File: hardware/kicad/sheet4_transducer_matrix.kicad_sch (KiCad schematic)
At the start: 0 parts

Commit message: feat: populate all 4 KiCad schematic sheets with embedded symbols and wiring
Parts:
- added TX1, TX10, TX11, TX12, TX13, TX14, TX15, TX16, TX17, TX18, TX19, TX2, TX20, TX21, TX22, TX23, TX24, TX25, TX26, TX27, TX28, TX29, TX3, TX30, TX31, TX32, TX33, TX34, TX35, TX36, TX37, TX38, TX39, TX4, TX40, TX41, TX42, TX43, TX44, TX45, TX46, TX47, TX48, TX49, TX5, TX50, TX51, TX52, TX53, TX54, TX55, TX56, TX57, TX58, TX59, TX6, TX60, TX61, TX62, TX63, TX64, TX7, TX8, TX9: 400ST160, symbol HPVE:Transducer_400ST
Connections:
- new net DRV_1: TX1.1 (+)
- new net DRV_10: TX10.1 (+)
- new net DRV_11: TX11.1 (+)
- new net DRV_12: TX12.1 (+)
- new net DRV_13: TX13.1 (+)
- new net DRV_14: TX14.1 (+)
- new net DRV_15: TX15.1 (+)
- new net DRV_16: TX16.1 (+)
- new net DRV_17: TX17.1 (+)
- new net DRV_18: TX18.1 (+)
- new net DRV_19: TX19.1 (+)
- new net DRV_2: TX2.1 (+)
- new net DRV_20: TX20.1 (+)
- new net DRV_21: TX21.1 (+)
- new net DRV_22: TX22.1 (+)
- new net DRV_23: TX23.1 (+)
- new net DRV_24: TX24.1 (+)
- new net DRV_25: TX25.1 (+)
- new net DRV_26: TX26.1 (+)
- new net DRV_27: TX27.1 (+)
- new net DRV_28: TX28.1 (+)
- new net DRV_29: TX29.1 (+)
- new net DRV_3: TX3.1 (+)
- new net DRV_30: TX30.1 (+)
- new net DRV_31: TX31.1 (+)
- new net DRV_32: TX32.1 (+)
- new net DRV_33: TX33.1 (+)
- new net DRV_34: TX34.1 (+)
- new net DRV_35: TX35.1 (+)
- new net DRV_36: TX36.1 (+)
- new net DRV_37: TX37.1 (+)
- new net DRV_38: TX38.1 (+)
- new net DRV_39: TX39.1 (+)
- new net DRV_4: TX4.1 (+)
- new net DRV_40: TX40.1 (+)
- new net DRV_41: TX41.1 (+)
- new net DRV_42: TX42.1 (+)
- new net DRV_43: TX43.1 (+)
- new net DRV_44: TX44.1 (+)
- new net DRV_45: TX45.1 (+)
- new net DRV_46: TX46.1 (+)
- new net DRV_47: TX47.1 (+)
- new net DRV_48: TX48.1 (+)
- new net DRV_49: TX49.1 (+)
- new net DRV_5: TX5.1 (+)
- new net DRV_50: TX50.1 (+)
- new net DRV_51: TX51.1 (+)
- new net DRV_52: TX52.1 (+)
- new net DRV_53: TX53.1 (+)
- new net DRV_54: TX54.1 (+)
- new net DRV_55: TX55.1 (+)
- new net DRV_56: TX56.1 (+)
- new net DRV_57: TX57.1 (+)
- new net DRV_58: TX58.1 (+)
- new net DRV_59: TX59.1 (+)
- new net DRV_6: TX6.1 (+)
- new net DRV_60: TX60.1 (+)
- new net DRV_61: TX61.1 (+)
- new net DRV_62: TX62.1 (+)
- new net DRV_63: TX63.1 (+)
- new net DRV_64: TX64.1 (+)
- new net DRV_7: TX7.1 (+)
- new net DRV_8: TX8.1 (+)
- new net DRV_9: TX9.1 (+)
- new net GND: TX1.2 (-), TX10.2 (-), TX11.2 (-), TX12.2 (-), TX13.2 (-), TX14.2 (-), TX15.2 (-), TX16.2 (-), TX17.2 (-), TX18.2 (-), TX19.2 (-), TX2.2 (-), TX20.2 (-), TX21.2 (-), TX22.2 (-), TX23.2 (-), TX24.2 (-), TX25.2 (-), TX26.2 (-), TX27.2 (-), TX28.2 (-), TX29.2 (-), TX3.2 (-), TX30.2 (-), TX31.2 (-), TX32.2 (-), TX33.2 (-), TX34.2 (-), TX35.2 (-), TX36.2 (-), TX37.2 (-), TX38.2 (-), TX39.2 (-), TX4.2 (-), TX40.2 (-), TX41.2 (-), TX42.2 (-), TX43.2 (-), TX44.2 (-), TX45.2 (-), TX46.2 (-), TX47.2 (-), TX48.2 (-), TX49.2 (-), TX5.2 (-), TX50.2 (-), TX51.2 (-), TX52.2 (-), TX53.2 (-), TX54.2 (-), TX55.2 (-), TX56.2 (-), TX57.2 (-), TX58.2 (-), TX59.2 (-), TX6.2 (-), TX60.2 (-), TX61.2 (-), TX62.2 (-), TX63.2 (-), TX64.2 (-), TX7.2 (-), TX8.2 (-), TX9.2 (-)
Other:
- title: Sheet 4: 8x8 Transducer Matrix Grid -> Sheet 4: 8x8 Transducer Matrix Grid (64 Elements)

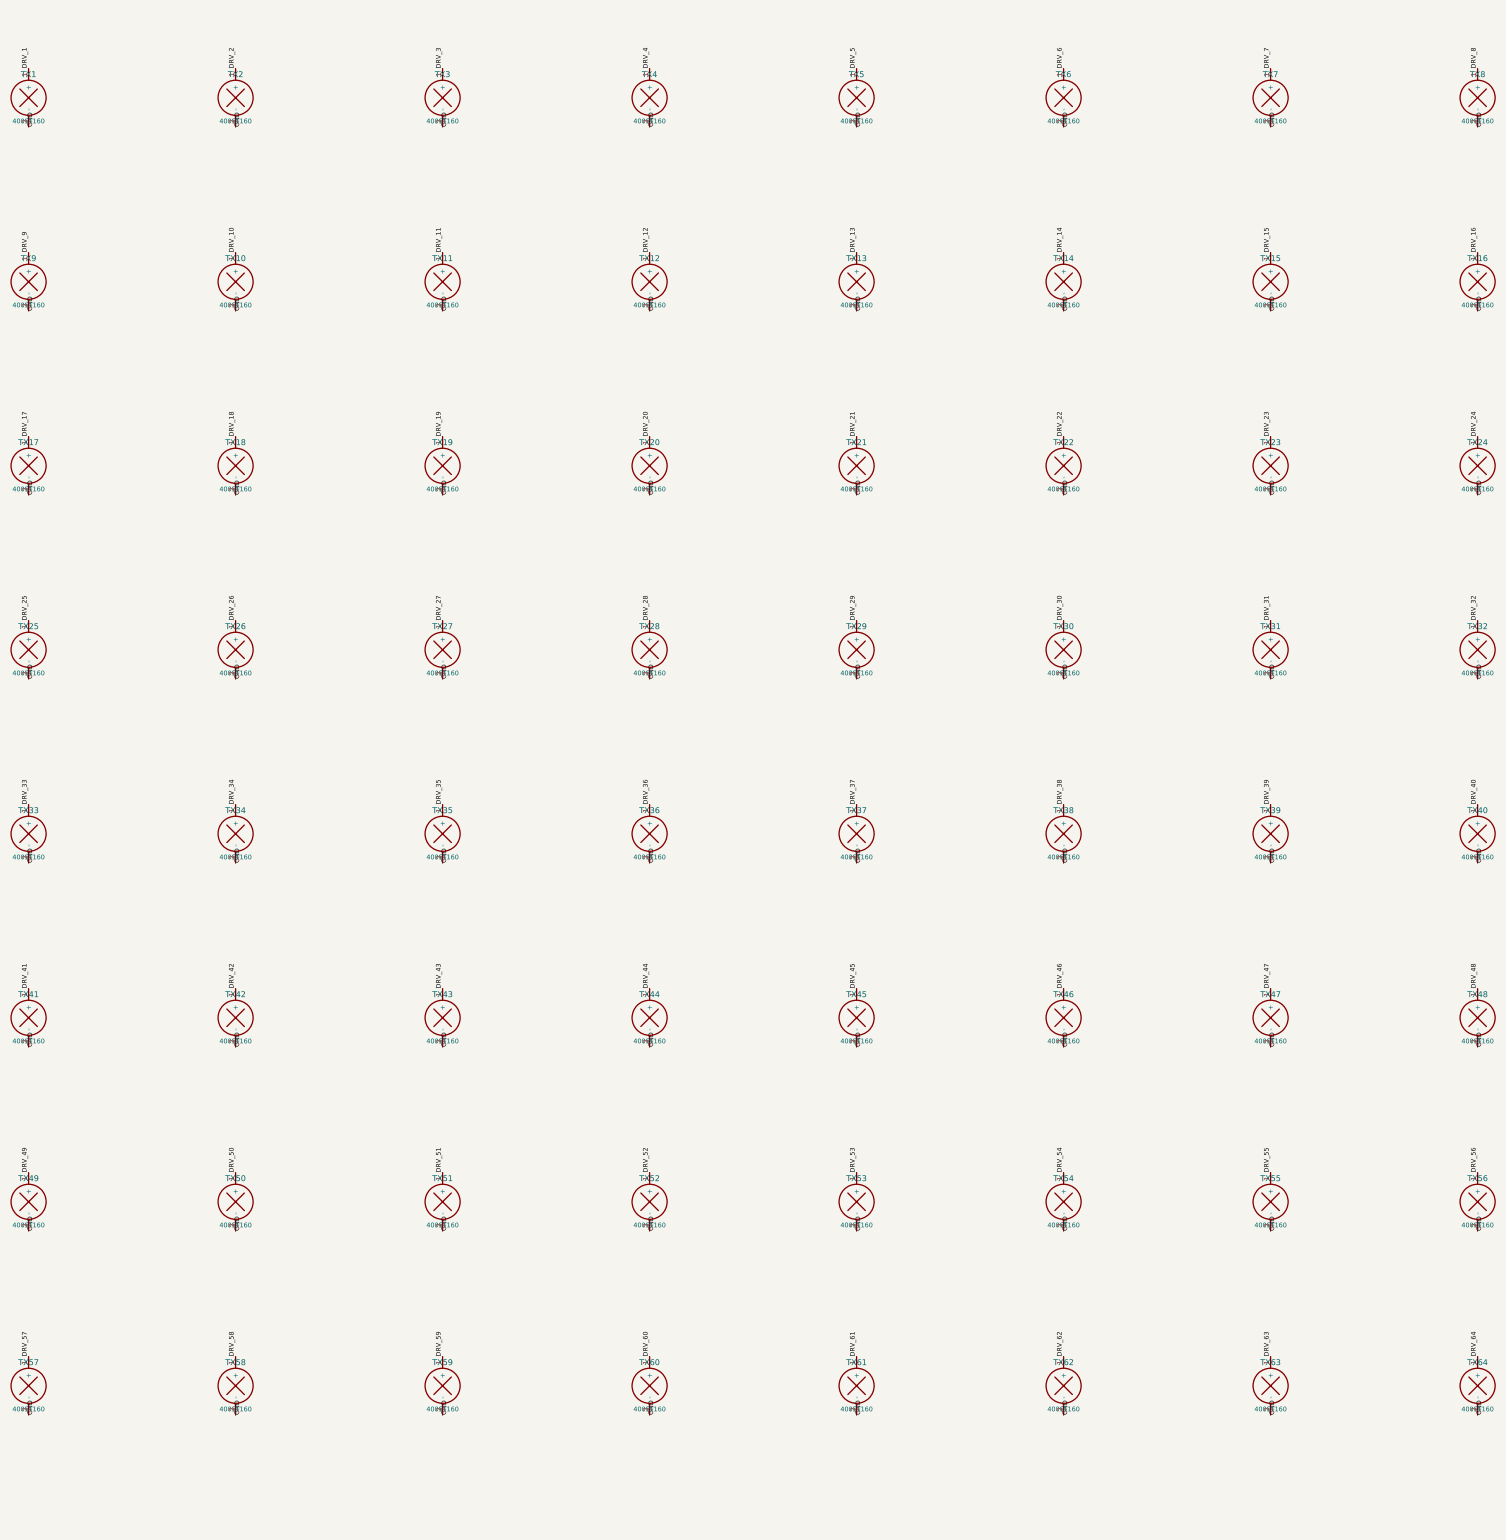
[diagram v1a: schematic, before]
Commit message: fix(kicad): assign valid footprints to all 105 symbols and add visible wiring
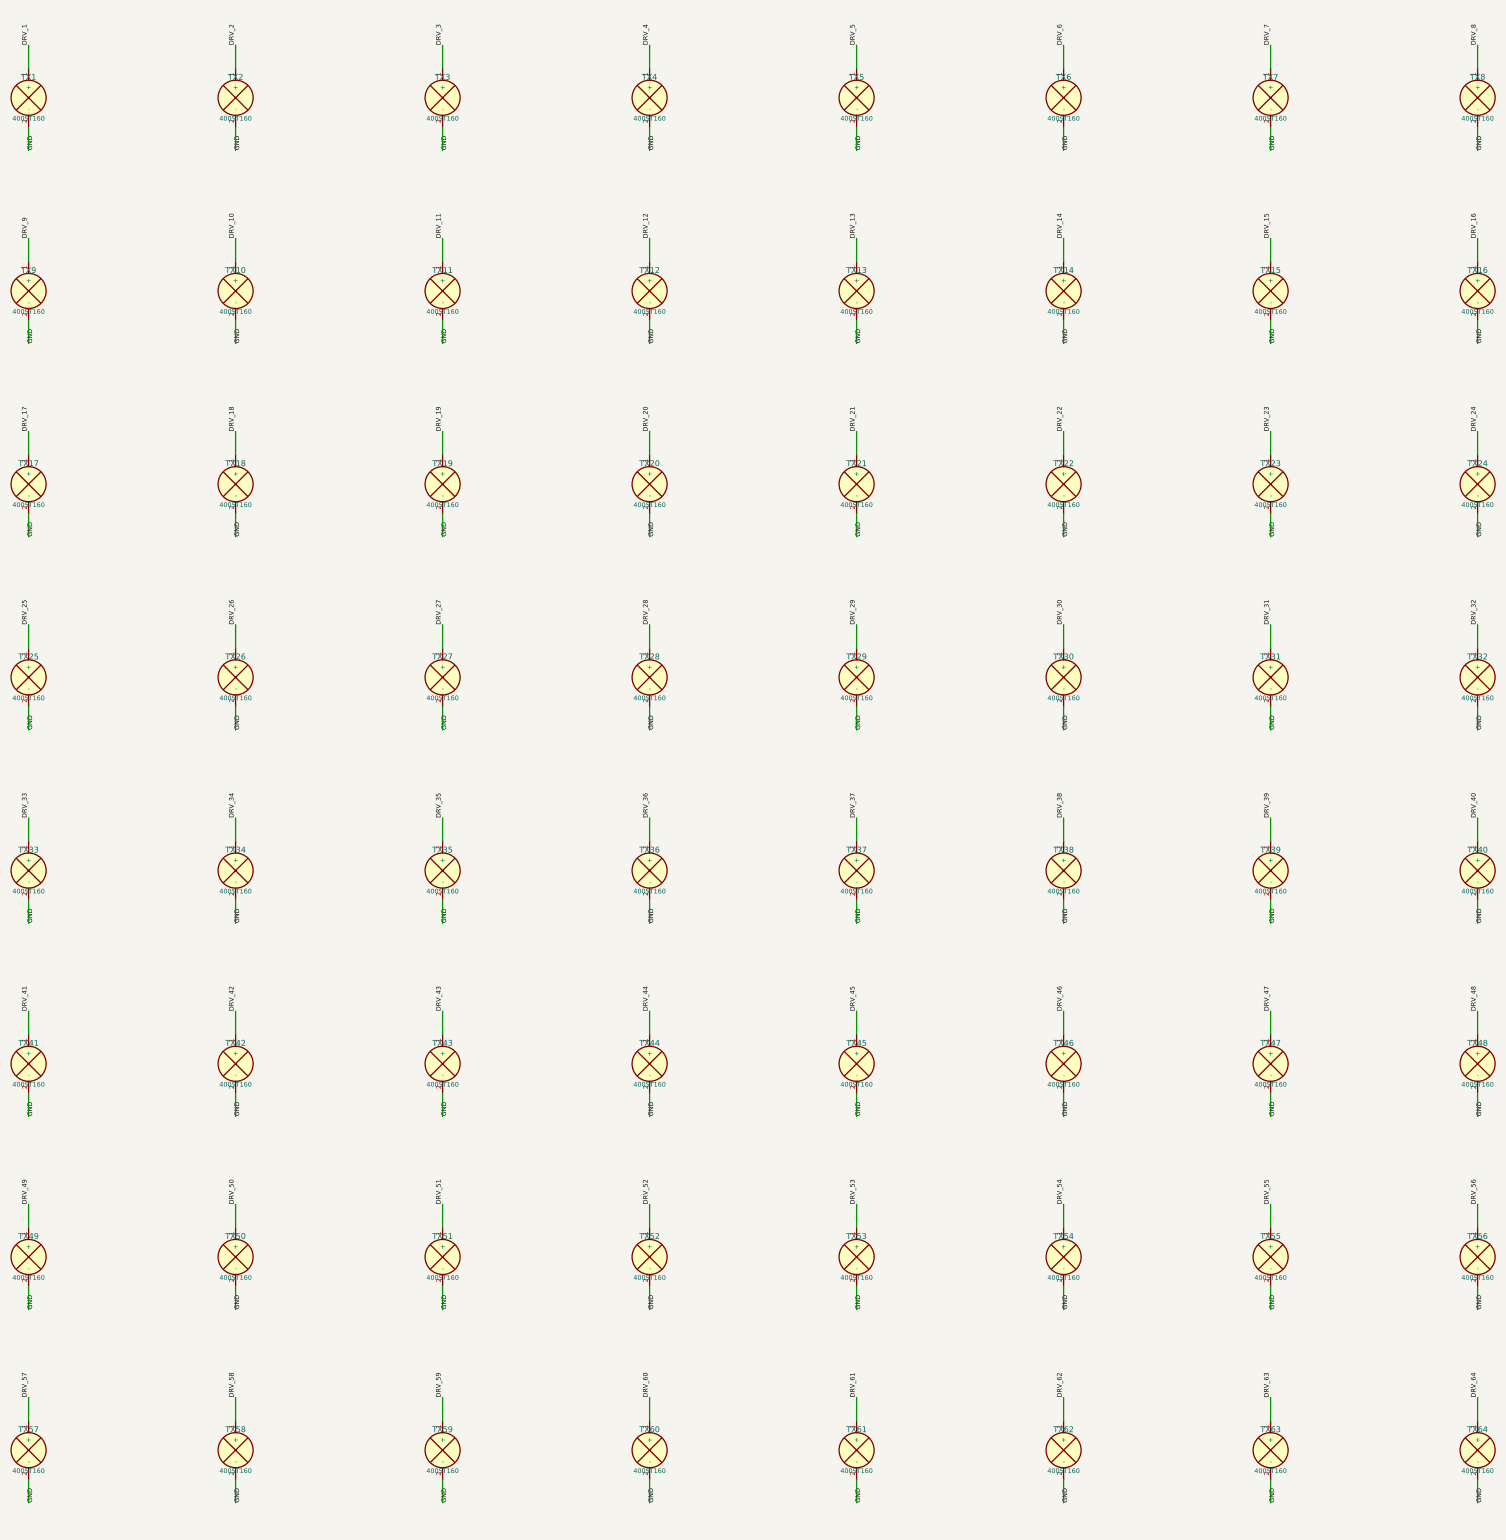
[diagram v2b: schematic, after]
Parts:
- TX1, TX10, TX11, TX12, TX13, TX14, TX15, TX16, TX17, TX18, TX19, TX2, TX20, TX21, TX22, TX23, TX24, TX25, TX26, TX27, TX28, TX29, TX3, TX30, TX31, TX32, TX33, TX34, TX35, TX36, TX37, TX38, TX39, TX4, TX40, TX41, TX42, TX43, TX44, TX45, TX46, TX47, TX48, TX49, TX5, TX50, TX51, TX52, TX53, TX54, TX55, TX56, TX57, TX58, TX59, TX6, TX60, TX61, TX62, TX63, TX64, TX7, TX8, TX9: footprint (none) -> Connector_PinHeader_2.54mm:PinHeader_1x02_P2.54mm_Vertical

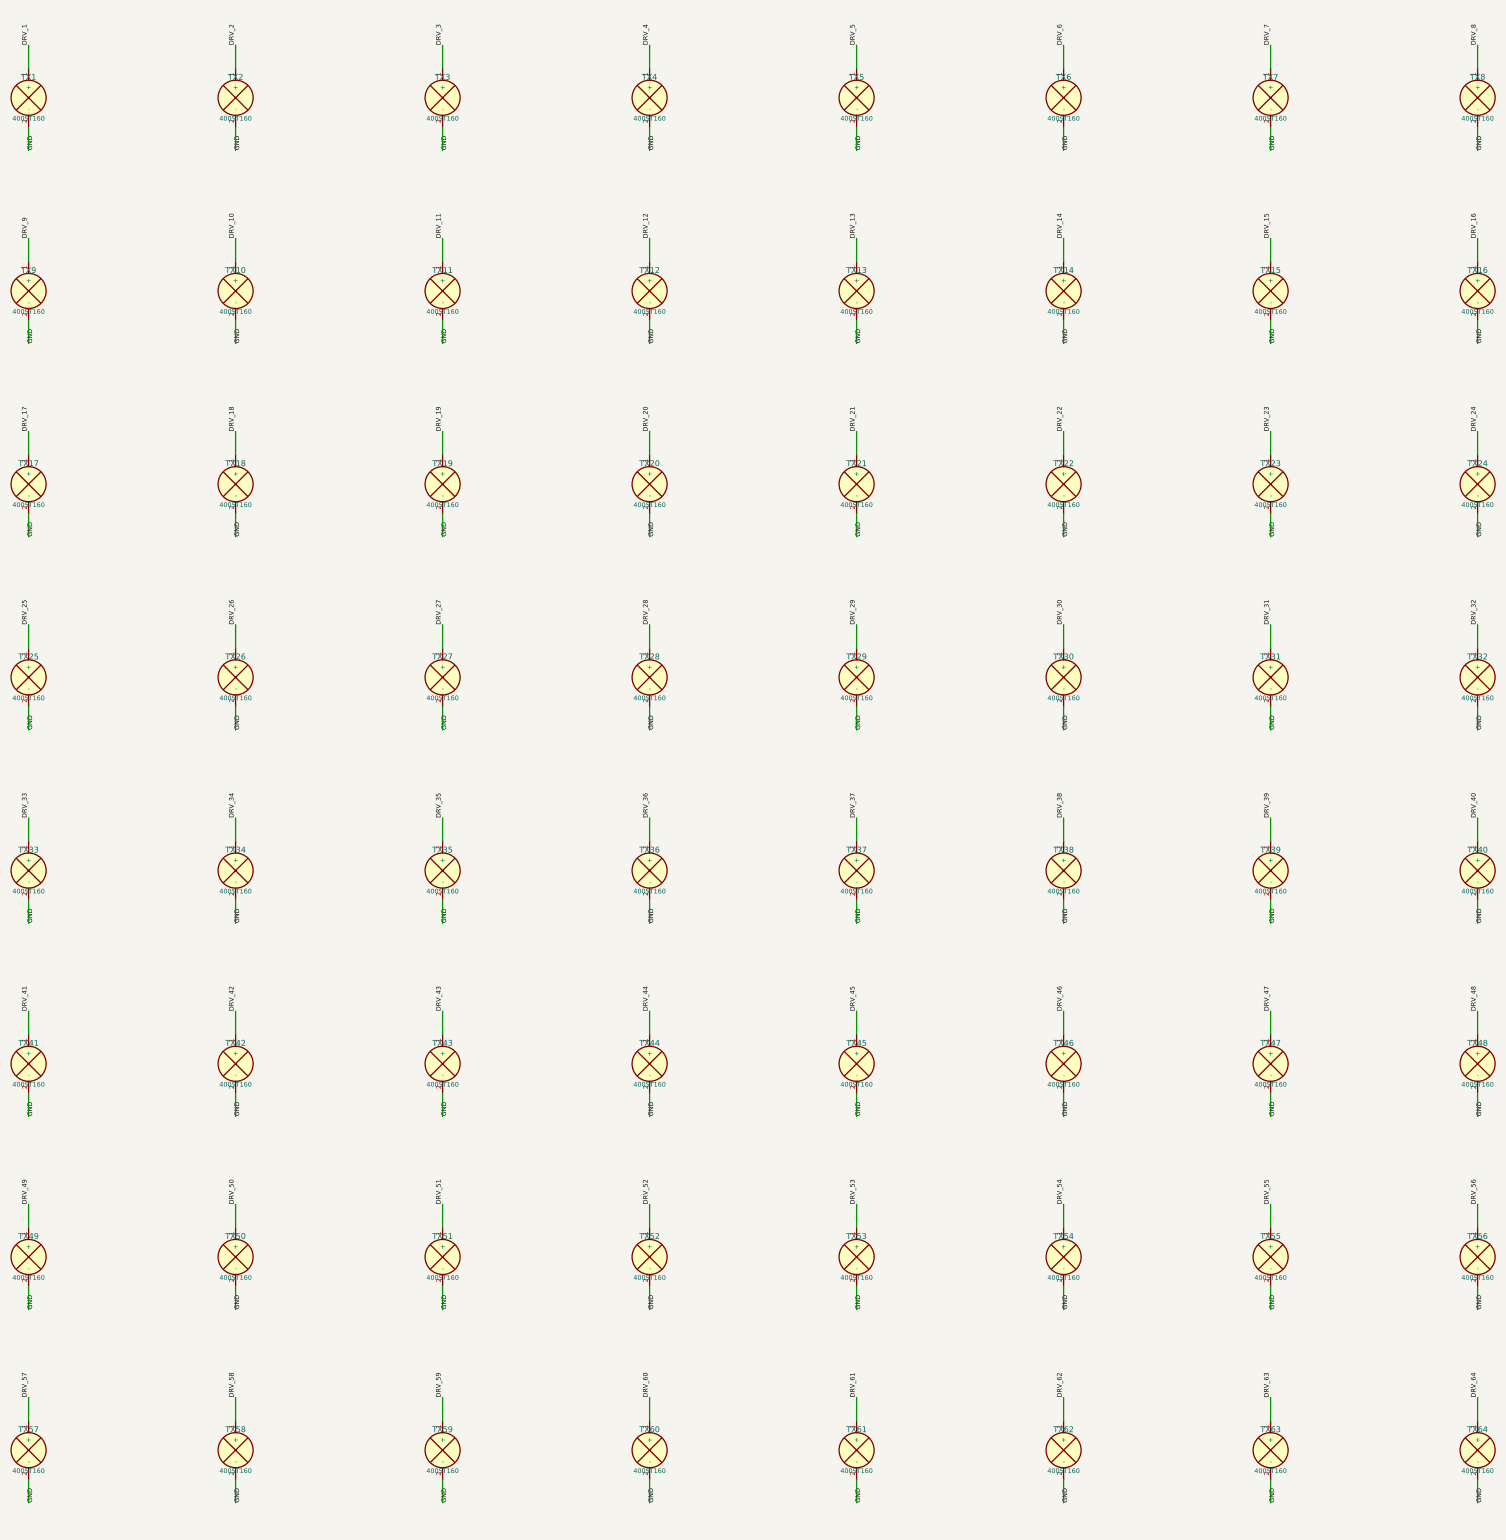
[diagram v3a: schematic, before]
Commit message: Auto-route 392 copper tracks for 64-channel HPVE phased array PCB
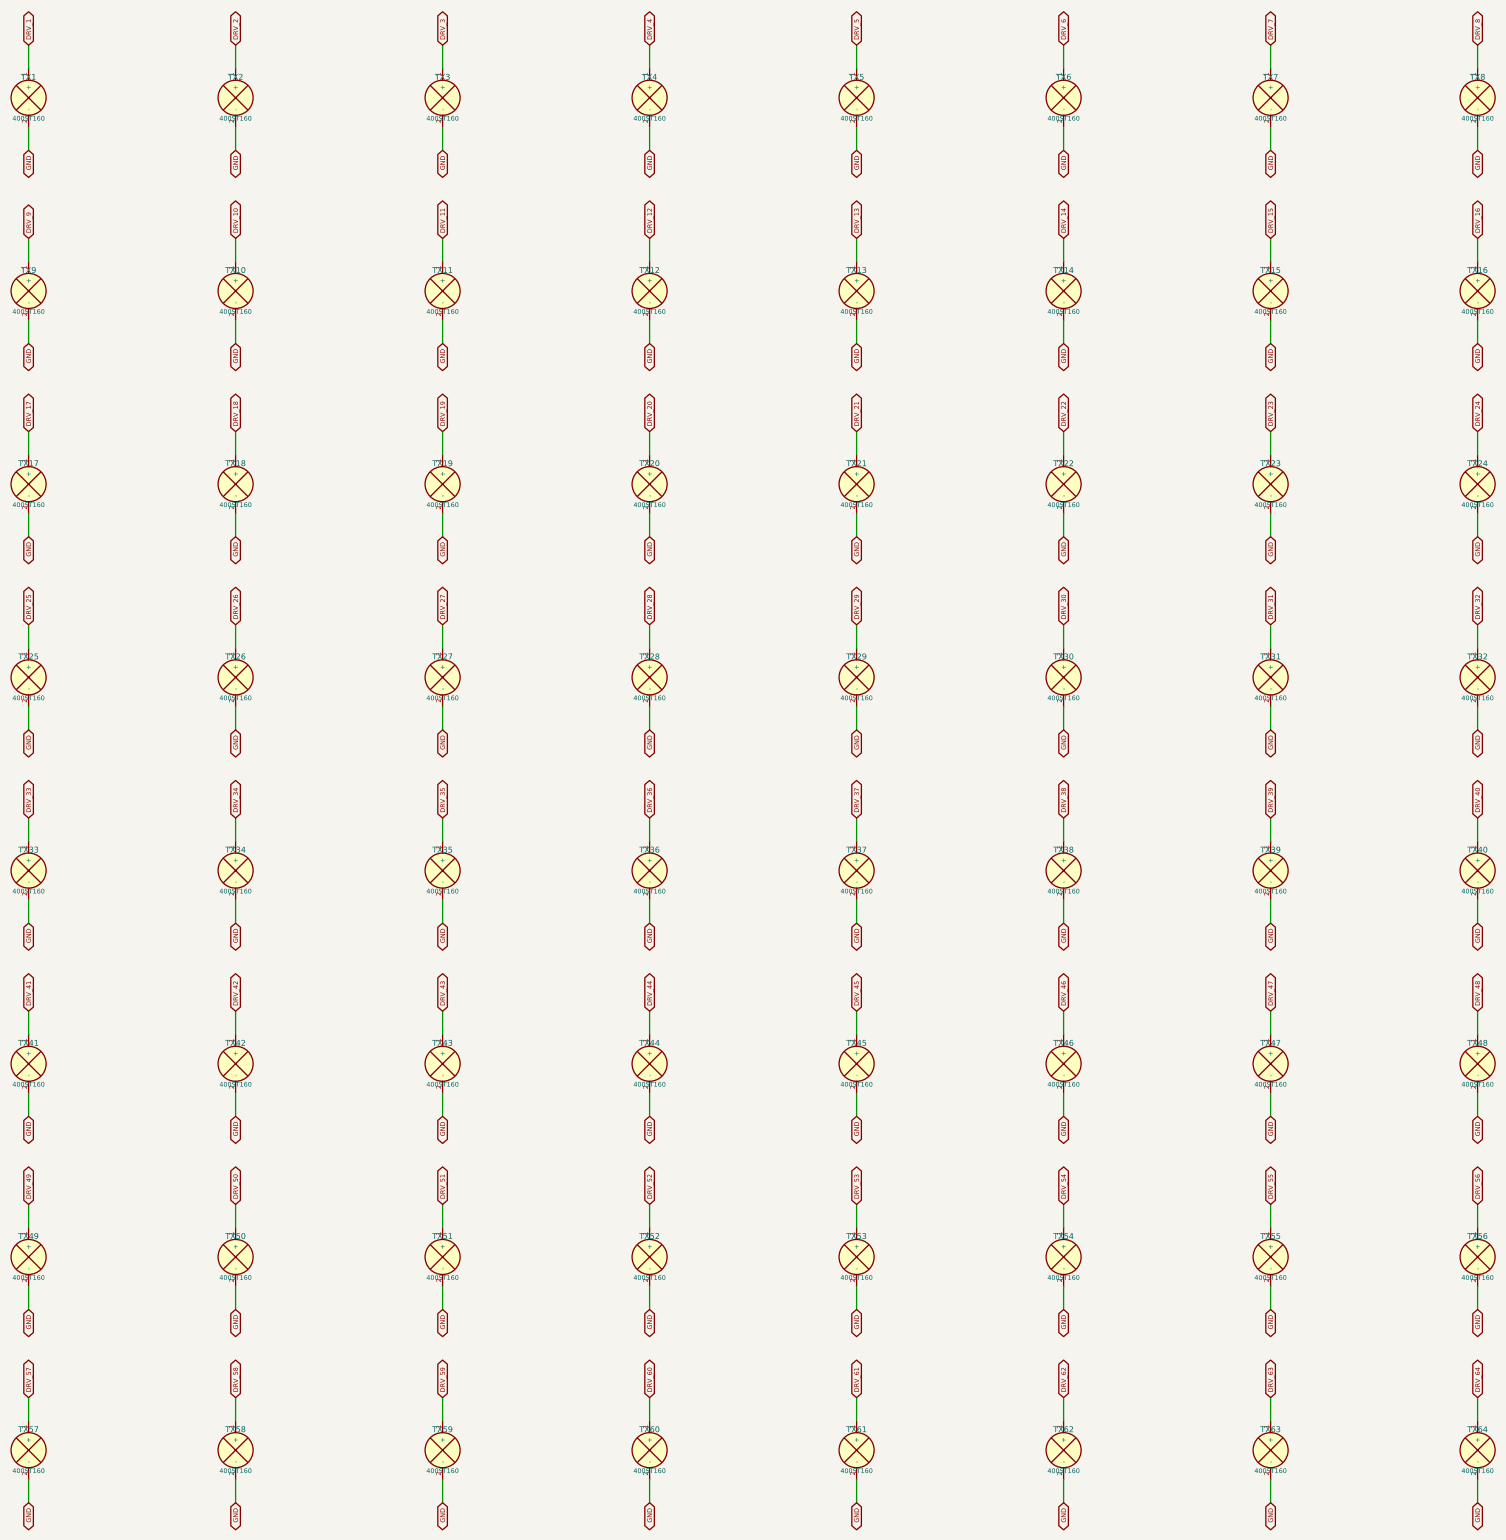
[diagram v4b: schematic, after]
